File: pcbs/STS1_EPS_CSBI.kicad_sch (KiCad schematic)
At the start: 2 parts

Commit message: Worked on STS1_EPS_1.
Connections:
- net at CSBI_2.19 (Pin_19): no longer CSBI_2.20 (Pin_20)
- net EPS_ANT_DEPLOYED: no longer names the net of CSBI_2.23 (Pin_23)
- net EPS_ANT_DEPLOYED: no longer CSBI_2.24 (Pin_24)
- no-connect marks 15 -> 16
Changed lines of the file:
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@@
   (no_connect (at 165.1 55.88))
   (no_connect (at 87.63 74.93))
+  (no_connect (at 177.8 66.04))
   (no_connect (at 87.63 82.55))
-  (no_connect (at 142.24 93.98))
   (no_connect (at 165.1 60.96))
   (no_connect (at 165.1 66.04))
@@
   (no_connect (at 87.63 87.63))
   (no_connect (at 139.7 53.34))
-  (no_connect (at 62.23 78.74))
+  (no_connect (at 165.1 71.12))
+  (no_connect (at 177.8 71.12))
   (bus_entry (at 149.86 93.98) (size 2.54 -2.54)
     (stroke (width 0) (type default) (color 0 0 0 0))
@@
     (stroke (width 0) (type default) (color 0 0 0 0))
   )
-  (wire (pts (xy 165.1 71.12) (xy 177.8 71.12))
-    (stroke (width 0) (type default) (color 0 0 0 0))
-  )
   (wire (pts (xy 87.63 52.07) (xy 100.33 52.07))
     (stroke (width 0) (type default) (color 0 0 0 0))
@@
   )
   (wire (pts (xy 87.63 67.31) (xy 100.33 67.31))
-    (stroke (width 0) (type default) (color 0 0 0 0))
-  )
-  (wire (pts (xy 165.1 66.04) (xy 177.8 66.04))
     (stroke (width 0) (type default) (color 0 0 0 0))
   )
@@
     (effects (font (size 1.27 1.27)) (justify left bottom))
   )
-  (hierarchical_label "EPS_ANT_DEPLOYED" (shape input) (at 165.1 71.12 180)
-    (effects (font (size 1.27 1.27)) (justify right))
-  )
   (hierarchical_label "VOUT" (shape input) (at 154.94 96.52 180)
     (effects (font (size 1.27 1.27)) (justify right))
@@
   )
   (hierarchical_label "EPS_CHARGING" (shape input) (at 165.1 73.66 180)
+    (effects (font (size 1.27 1.27)) (justify right))
+  )
+  (hierarchical_label "COBC_SPI_[1..6]" (shape bidirectional) (at 142.24 93.98 180)
+    (effects (font (size 1.27 1.27)) (justify right))
+  )
+  (hierarchical_label "EDU_SPI_[1..6]" (shape bidirectional) (at 62.23 78.74 180)
     (effects (font (size 1.27 1.27)) (justify right))
   )
@@
   (symbol (lib_id "power:GND") (at 87.63 44.45 270) (unit 1)
     (in_bom yes) (on_board yes)
-    (property "Reference" "#PWR0105" (id 0) (at 81.28 44.45 0)
+    (property "Reference" "#PWR019" (id 0) (at 81.28 44.45 0)
       (effects (font (size 1.27 1.27)) hide)
     )
@@
   (symbol (lib_id "power:GND") (at 87.63 46.99 270) (unit 1)
     (in_bom yes) (on_board yes)
-    (property "Reference" "#PWR0106" (id 0) (at 81.28 46.99 0)
+    (property "Reference" "#PWR020" (id 0) (at 81.28 46.99 0)
       (effects (font (size 1.27 1.27)) hide)
     )
@@
   (symbol (lib_id "power:GND") (at 87.63 54.61 270) (unit 1)
     (in_bom yes) (on_board yes)
-    (property "Reference" "#PWR0109" (id 0) (at 81.28 54.61 0)
+    (property "Reference" "#PWR021" (id 0) (at 81.28 54.61 0)
       (effects (font (size 1.27 1.27)) hide)
     )
@@
   (symbol (lib_id "power:GND") (at 87.63 85.09 270) (unit 1)
     (in_bom yes) (on_board yes)
-    (property "Reference" "#PWR0111" (id 0) (at 81.28 85.09 0)
+    (property "Reference" "#PWR023" (id 0) (at 81.28 85.09 0)
       (effects (font (size 1.27 1.27)) hide)
     )
@@
   (symbol (lib_id "power:GND") (at 87.63 102.87 270) (unit 1)
     (in_bom yes) (on_board yes)
-    (property "Reference" "#PWR0113" (id 0) (at 81.28 102.87 0)
+    (property "Reference" "#PWR025" (id 0) (at 81.28 102.87 0)
       (effects (font (size 1.27 1.27)) hide)
     )
@@
   (symbol (lib_id "power:GND") (at 87.63 105.41 270) (unit 1)
     (in_bom yes) (on_board yes)
-    (property "Reference" "#PWR0114" (id 0) (at 81.28 105.41 0)
+    (property "Reference" "#PWR026" (id 0) (at 81.28 105.41 0)
       (effects (font (size 1.27 1.27)) hide)
     )
@@
   (symbol (lib_id "power:GND") (at 165.1 43.18 270) (unit 1)
     (in_bom yes) (on_board yes)
-    (property "Reference" "#PWR0115" (id 0) (at 158.75 43.18 0)
+    (property "Reference" "#PWR027" (id 0) (at 158.75 43.18 0)
       (effects (font (size 1.27 1.27)) hide)
     )
@@
   (symbol (lib_id "power:GND") (at 165.1 45.72 270) (unit 1)
     (in_bom yes) (on_board yes)
-    (property "Reference" "#PWR0116" (id 0) (at 158.75 45.72 0)
+    (property "Reference" "#PWR028" (id 0) (at 158.75 45.72 0)
       (effects (font (size 1.27 1.27)) hide)
     )
@@
   (symbol (lib_id "power:GND") (at 165.1 104.14 270) (unit 1)
     (in_bom yes) (on_board yes)
-    (property "Reference" "#PWR0117" (id 0) (at 158.75 104.14 0)
+    (property "Reference" "#PWR034" (id 0) (at 158.75 104.14 0)
       (effects (font (size 1.27 1.27)) hide)
     )
@@
   (symbol (lib_id "power:GND") (at 165.1 101.6 270) (unit 1)
     (in_bom yes) (on_board yes)
-    (property "Reference" "#PWR0118" (id 0) (at 158.75 101.6 0)
+    (property "Reference" "#PWR033" (id 0) (at 158.75 101.6 0)
       (effects (font (size 1.27 1.27)) hide)
     )
@@
   (symbol (lib_id "power:GND") (at 165.1 76.2 270) (unit 1)
     (in_bom yes) (on_board yes)
-    (property "Reference" "#PWR0119" (id 0) (at 158.75 76.2 0)
+    (property "Reference" "#PWR031" (id 0) (at 158.75 76.2 0)
       (effects (font (size 1.27 1.27)) hide)
     )
@@
   (symbol (lib_id "power:GND") (at 165.1 63.5 270) (unit 1)
     (in_bom yes) (on_board yes)
-    (property "Reference" "#PWR0120" (id 0) (at 158.75 63.5 0)
+    (property "Reference" "#PWR030" (id 0) (at 158.75 63.5 0)
       (effects (font (size 1.27 1.27)) hide)
     )
@@
   (symbol (lib_id "power:GND") (at 165.1 93.98 270) (unit 1)
     (in_bom yes) (on_board yes)
-    (property "Reference" "#PWR0121" (id 0) (at 158.75 93.98 0)
+    (property "Reference" "#PWR032" (id 0) (at 158.75 93.98 0)
       (effects (font (size 1.27 1.27)) hide)
     )
@@
   (symbol (lib_id "power:GND") (at 87.63 72.39 270) (unit 1)
     (in_bom yes) (on_board yes)
-    (property "Reference" "#PWR0110" (id 0) (at 81.28 72.39 0)
+    (property "Reference" "#PWR022" (id 0) (at 81.28 72.39 0)
       (effects (font (size 1.27 1.27)) hide)
     )
@@
   (symbol (lib_id "power:GND") (at 87.63 95.25 270) (unit 1)
     (in_bom yes) (on_board yes)
-    (property "Reference" "#PWR0112" (id 0) (at 81.28 95.25 0)
+    (property "Reference" "#PWR024" (id 0) (at 81.28 95.25 0)
       (effects (font (size 1.27 1.27)) hide)
     )
@@
   (symbol (lib_id "power:GND") (at 165.1 53.34 270) (unit 1)
     (in_bom yes) (on_board yes)
-    (property "Reference" "#PWR0124" (id 0) (at 158.75 53.34 0)
-      (effects (font (size 1.27 1.27)) hide)
-    )
+    (property "Reference" "#PWR029" (id 0) (at 158.75 53.34 0)
+      (effects (font (size 1.27 1.27)) hide)
+    )

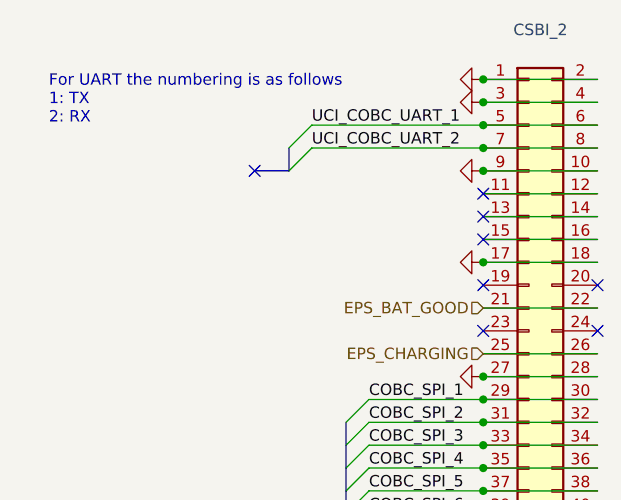
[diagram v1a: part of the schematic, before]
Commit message: Worked on STS1_EPS_1.
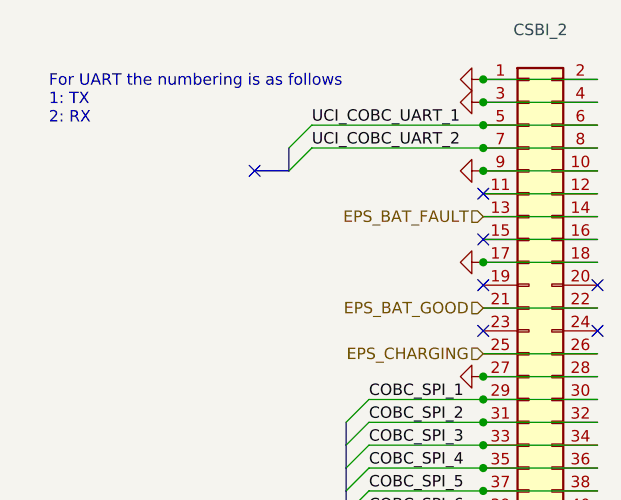
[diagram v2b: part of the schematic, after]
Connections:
- net EPS_BAT_FAULT: now reaches CSBI_2.13 (Pin_13), CSBI_2.14 (Pin_14)
- no-connect marks 16 -> 15
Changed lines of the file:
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@@
   (no_connect (at 87.63 80.01))
   (no_connect (at 87.63 77.47))
-  (no_connect (at 165.1 58.42))
   (no_connect (at 165.1 55.88))
   (no_connect (at 87.63 74.93))
@@
     (stroke (width 0) (type default) (color 0 0 0 0))
   )
+  (wire (pts (xy 165.1 58.42) (xy 177.8 58.42))
+    (stroke (width 0) (type default) (color 0 0 0 0))
+  )
   (bus (pts (xy 67.31 72.39) (xy 67.31 78.74))
     (stroke (width 0) (type default) (color 0 0 0 0))
@@
   )
   (wire (pts (xy 165.1 91.44) (xy 152.4 91.44))
-    (stroke (width 0) (type default) (color 0 0 0 0))
-  )
-  (wire (pts (xy 165.1 58.42) (xy 177.8 58.42))
     (stroke (width 0) (type default) (color 0 0 0 0))
   )
@@
     (effects (font (size 1.27 1.27)) (justify right))
   )
+  (hierarchical_label "EPS_BAT_FAULT" (shape input) (at 165.1 58.42 180)
+    (effects (font (size 1.27 1.27)) (justify right))
+  )

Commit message: Worked on STS_EPS_1.
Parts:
- CSBI_1, CSBI_2: footprint (none) -> Connector_PinHeader_2.00mm:PinHeader_2x25_P2.00mm_Vertical
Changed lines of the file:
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@@
     (property "Reference" "CSBI_1" (id 0) (at 93.98 38.9382 0))
     (property "Value" "~" (id 1) (at 93.98 41.2496 0))
-    (property "Footprint" "" (id 2) (at 92.71 74.93 0)
+    (property "Footprint" "Connector_PinHeader_2.00mm:PinHeader_2x25_P2.00mm_Vertical" (id 2) (at 92.71 74.93 0)
       (effects (font (size 1.27 1.27)) hide)
     )
@@
     (property "Reference" "CSBI_2" (id 0) (at 171.45 37.6682 0))
     (property "Value" "~" (id 1) (at 171.45 39.9796 0))
-    (property "Footprint" "" (id 2) (at 170.18 73.66 0)
+    (property "Footprint" "Connector_PinHeader_2.00mm:PinHeader_2x25_P2.00mm_Vertical" (id 2) (at 170.18 73.66 0)
       (effects (font (size 1.27 1.27)) hide)
     )
